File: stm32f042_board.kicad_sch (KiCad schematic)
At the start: 24 parts, among them J1 Conn_01x12_Female, J2 Conn_01x12_Female, J3 USB_B_Micro, J5 JTAG/SWD, U1 STM32F042F6Px, U2 MCP1802, U3 USBLC6-2SC6

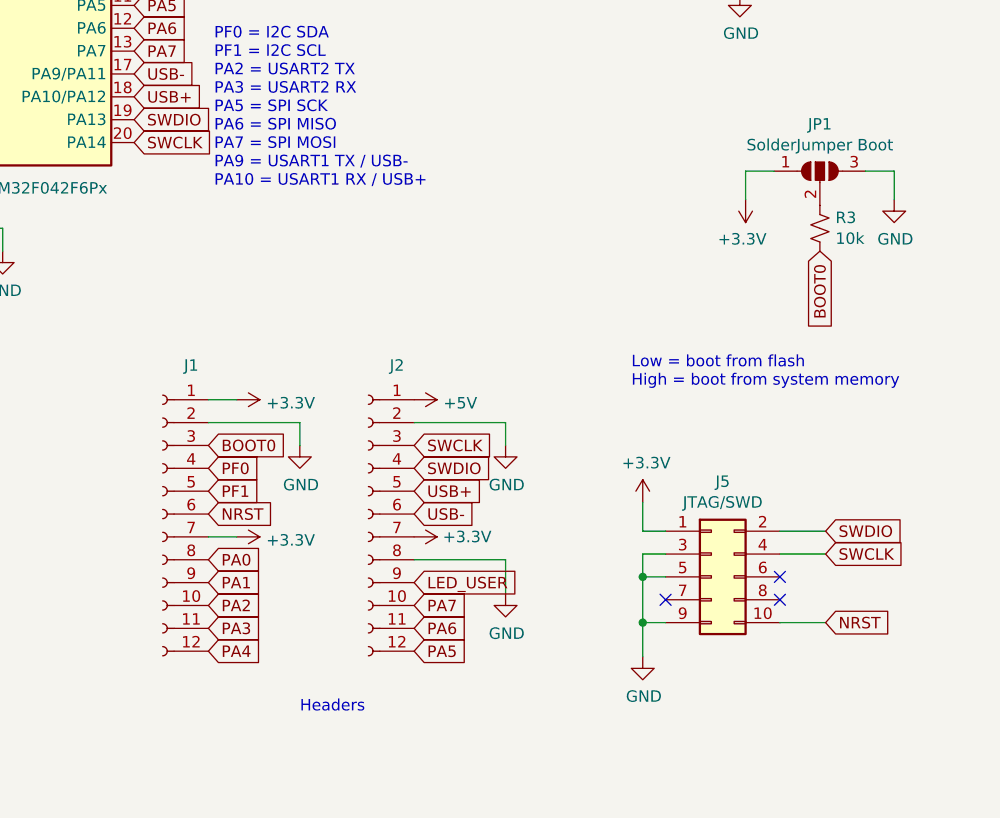
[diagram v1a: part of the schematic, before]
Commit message: Revert "Migrate to KiCad 7"
This reverts commit a80925b01a00ac2b6e233b577ff1a59522959ffa.

- Footprints and some other things don't seem to work right yet
- OSHPark not v7 compatible yet.
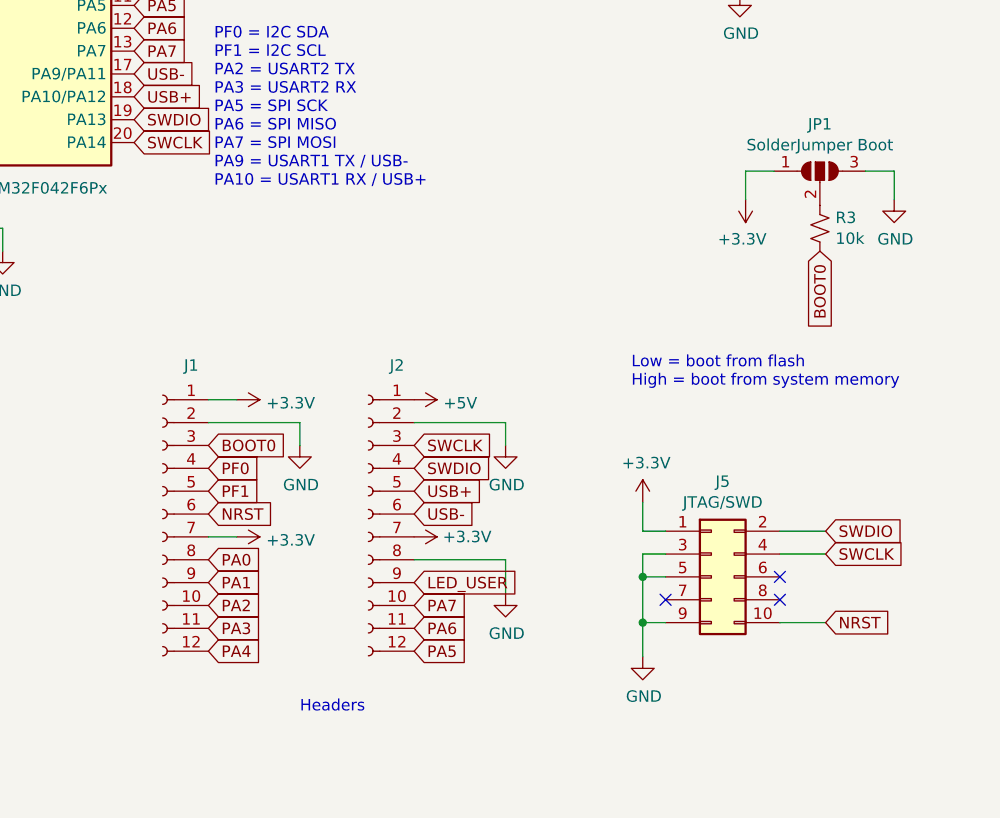
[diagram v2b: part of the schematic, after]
